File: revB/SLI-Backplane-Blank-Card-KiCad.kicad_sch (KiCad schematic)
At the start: 1 part, among them P201 Conn_02x60_Top_Bottom

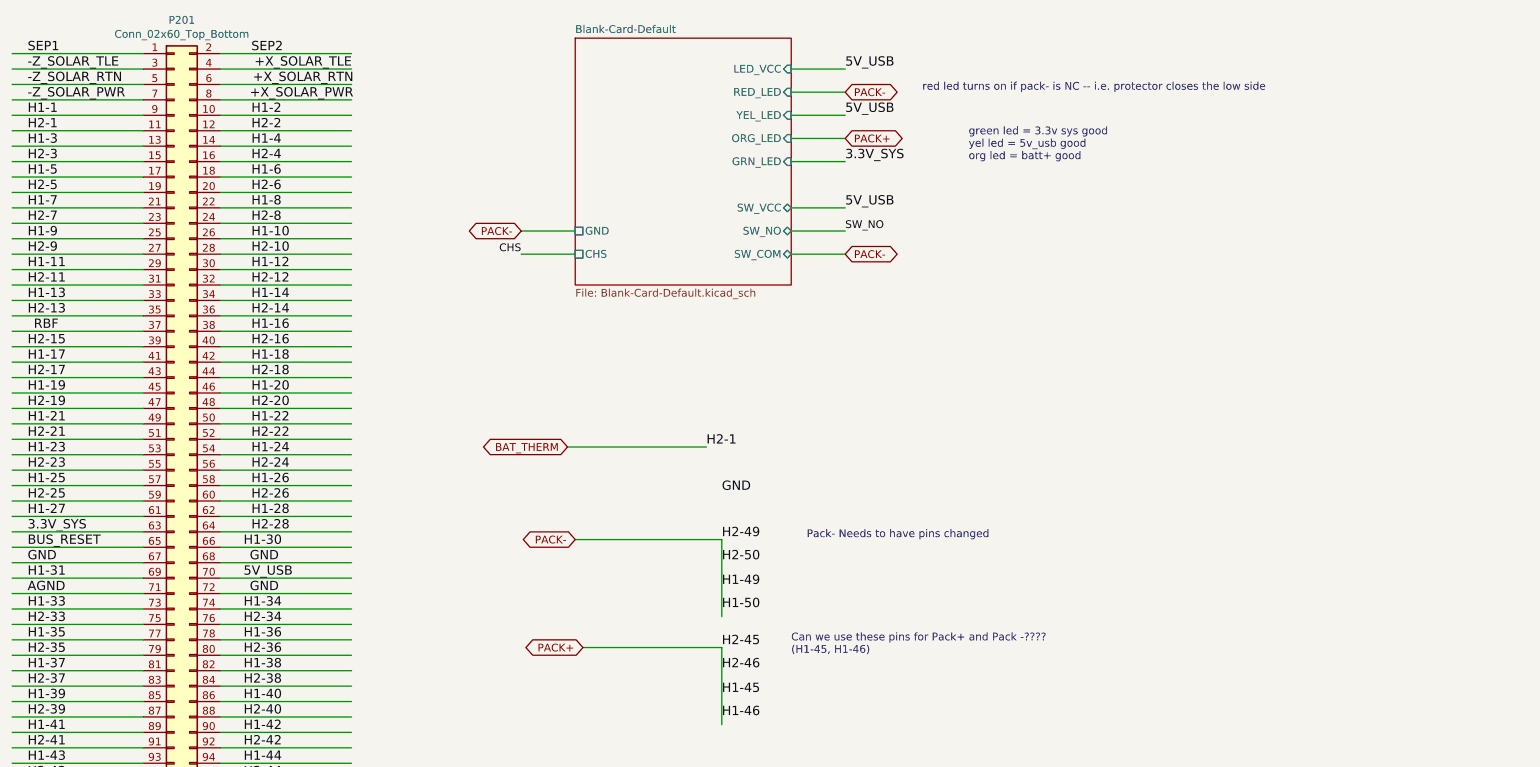
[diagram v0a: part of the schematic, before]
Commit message: update project to kicad 7 format
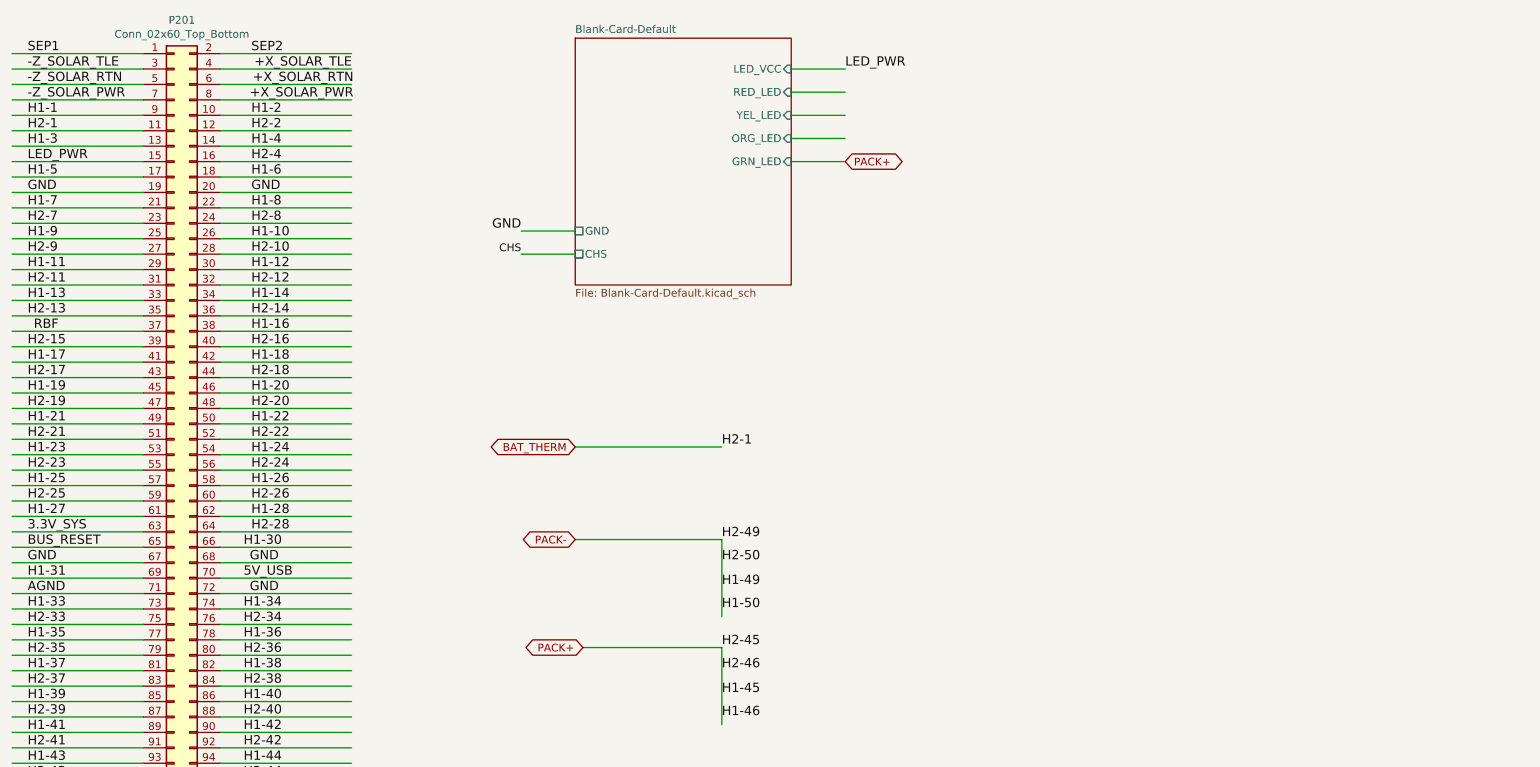
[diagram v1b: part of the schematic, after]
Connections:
- net H2-5 is gone; now on net GND: P201.19 (Pin_19)
- net H2-6 is gone; now on net GND: P201.20 (Pin_20)
- net H2-3 renamed LED_PWR
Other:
- sheet Blank-Card-Default ports: added none; removed SW_COM, SW_NO, SW_VCC
- note removed: "Can we use these pins for Pack+ and Pack -???? (H1-45, H1-46)"
- note removed: "Pack- Needs to have pins changed"
- note removed: "green led = 3.3v sys good yel led = 5v_usb good org led = batt+ good"
- note removed: "red led turns on if pack- is NC -- i.e. protector closes the low side"
